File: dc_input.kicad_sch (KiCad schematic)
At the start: 15 parts, among them J1 S2B-PH-SM4, J3 USB4125-GF-A, U3 LM66200, U8 TLV76701DRVx

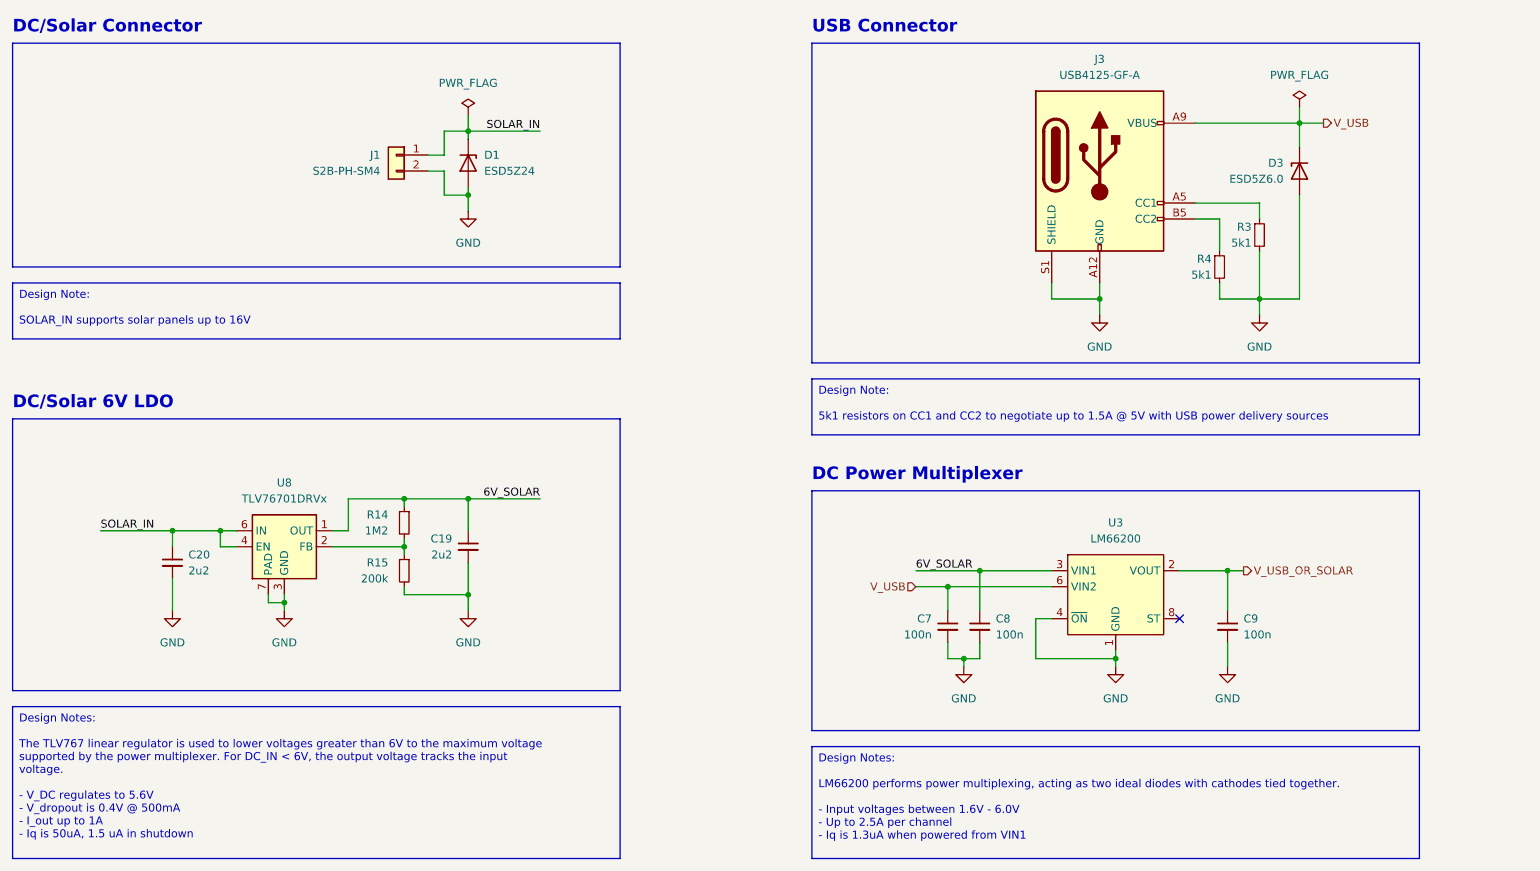
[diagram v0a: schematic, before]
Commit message: update to kicad 9.0
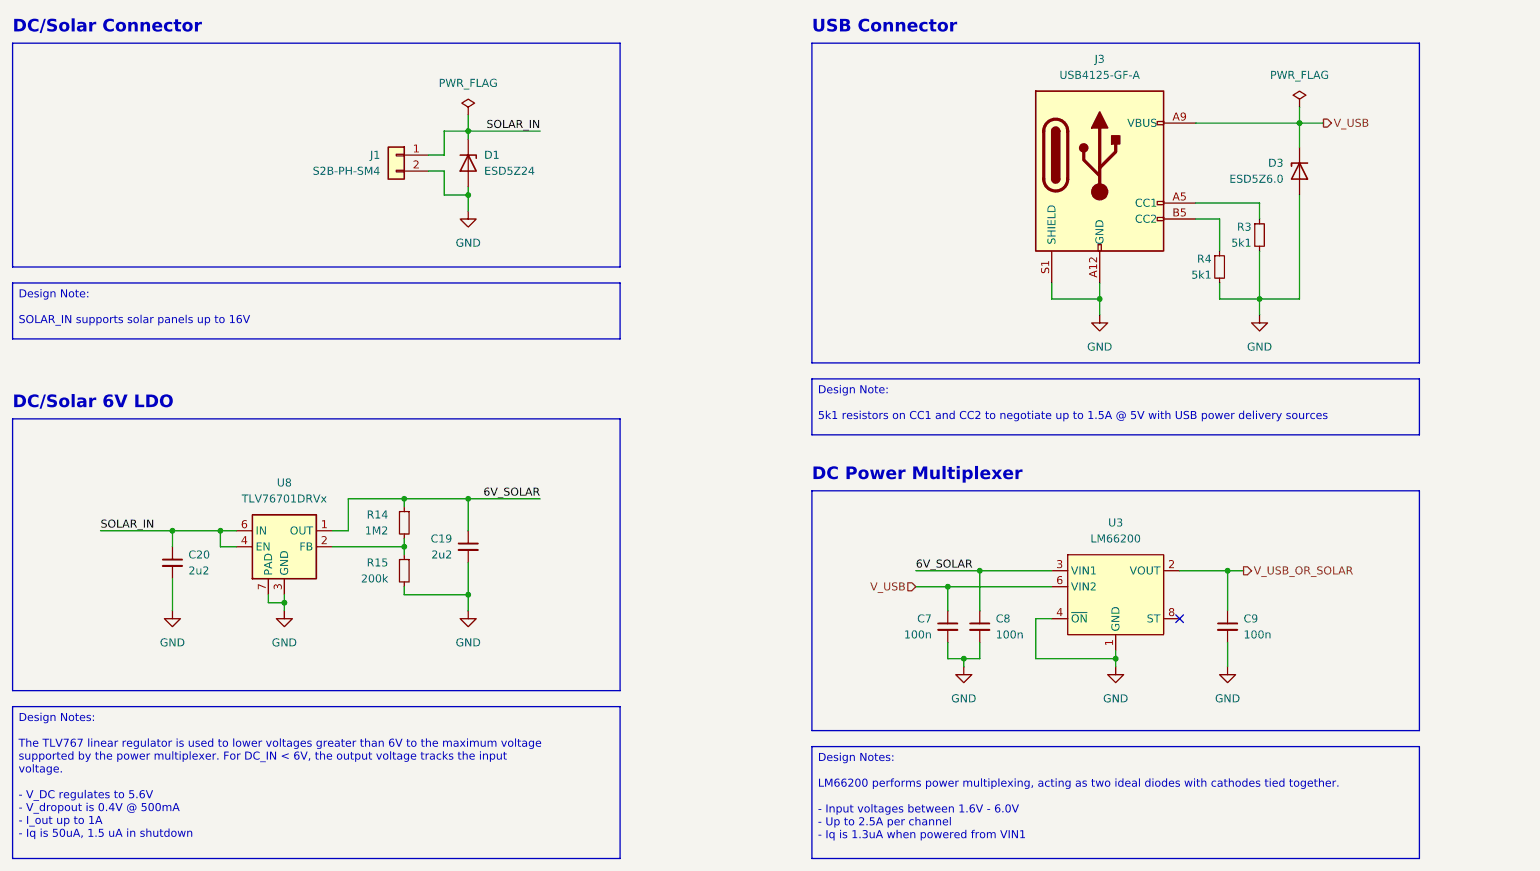
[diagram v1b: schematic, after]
